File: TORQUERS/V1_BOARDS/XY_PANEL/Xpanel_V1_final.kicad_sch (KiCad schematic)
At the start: 68 parts, among them J2 F3311A7H121014E200, Q1 BSS138, Q10 BSS138, Q11 BSS138, Q13 BSS138, Q14 BSS138, Q2 BSS138, Q4 BSS138, Q5 BSS138, U1 DRV8830DGQ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

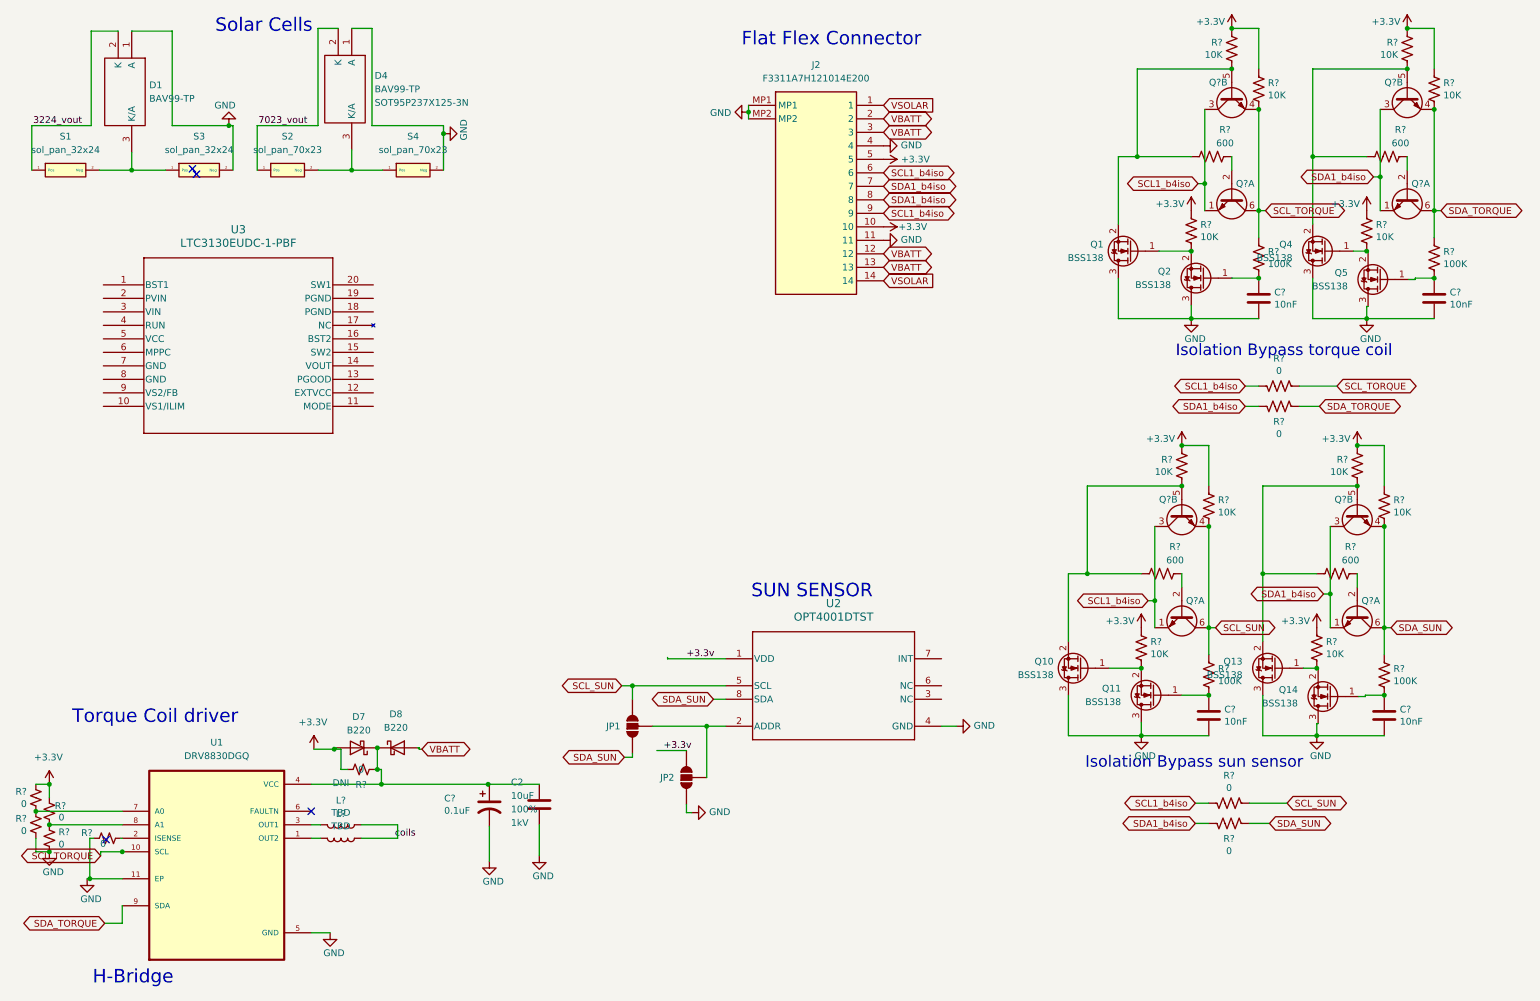
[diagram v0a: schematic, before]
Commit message: Made changes to LTC ; remaining switches for H bridge and  LTC3130 for 70mm panel
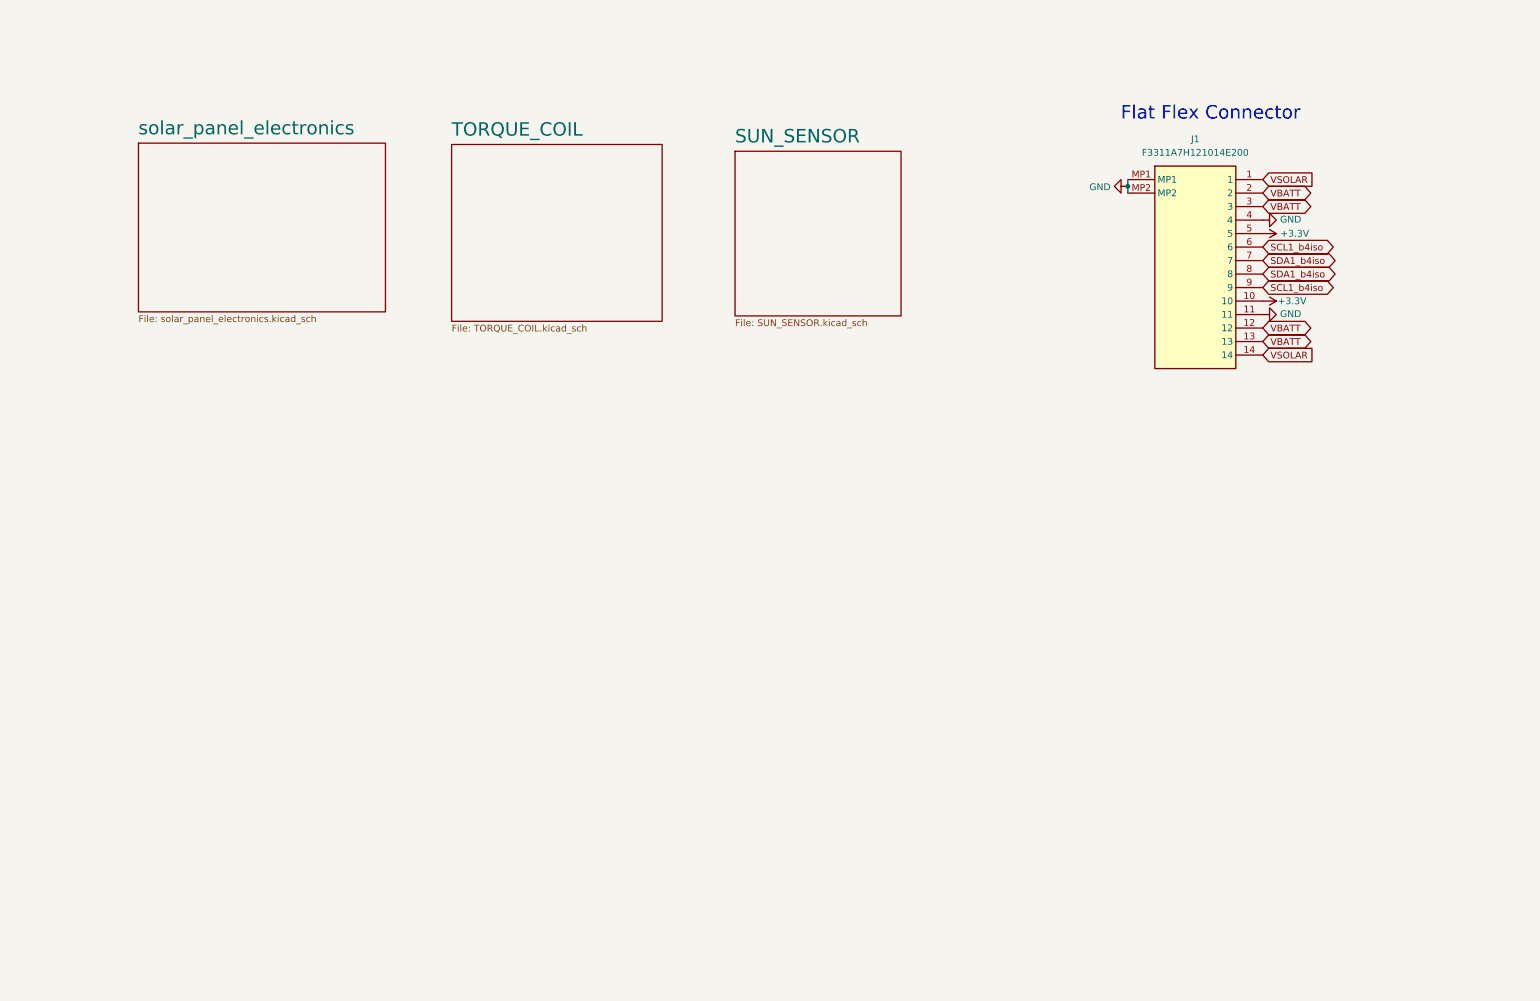
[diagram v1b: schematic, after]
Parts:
- removed C2: 10uF, Capacitor_SMD:C_0805_2012Metric, symbol SparkFun-Capacitor:C_Polarized
- removed C? (x4): 10nF, Capacitor_SMD:C_0603_1608Metric, symbol Device:C
- removed C?: 0.1uF, Capacitor_SMD:C_0402_1005Metric, symbol Device:C
- removed D1, D4: BAV99-TP, SOT95P237X125-3N, symbol AA_AUTO_LOADER:BAV99-TP
- removed D7, D8: B220, Diode_SMD:D_SMB, symbol Diode:B220
- removed J2: F3311A7H121014E200, F3311A7H121014E200, symbol F3311A7H121008E200:F3311A7H121014E200
- removed JP1, JP2: ~, SparkFun-Jumper:SMT-JUMPER_3_NO_NO-SILK, symbol SparkFun-Jumper:SolderJumper_3_Open_No_Silk
- removed L? (x2): TBD, Inductor_SMD:L_0603_1608Metric, symbol Device:L
- removed Q1, Q10, Q11, Q13, Q14, Q2, Q4, Q5: BSS138, Package_TO_SOT_SMD:SOT-23, symbol Transistor_FET:BSS138
- removed Q? (x8): MBT2222ADW1T1, Package_TO_SOT_SMD:SOT-363_SC-70-6, symbol Transistor_BJT:MBT2222ADW1T1
- removed R? (x5): 0, Resistor_SMD:R_0402_1005Metric, symbol Device:R_Small_US
- removed R? (x4): 600, Resistor_SMD:R_0603_1608Metric, symbol Device:R_US
- removed R? (x8): 10K, Resistor_SMD:R_0603_1608Metric, symbol Device:R_US
- removed R?: 0, Resistor_SMD:R_0603_1608Metric, symbol Device:R_Small_US
- removed R? (x4): 0, Resistor_SMD:R_0603_1608Metric, symbol Device:R_US
- removed R? (x4): 100K, Resistor_SMD:R_0603_1608Metric, symbol Device:R_US
- removed R? (x4): 10K, Resistor_SMD:R_0402_1005Metric, symbol Device:R_US
- removed S1, S3: sol_pan_32x24, CUSTOM_SOLAR_2432:solar_panel_SM500K12TF_32x24, symbol solar_symbol_lib:sol_pan_32x24
- removed S2, S4: sol_pan_70x23, CUSTOM_SOLAR_7023:sol_pan_SM141K10TFS_70x23, symbol solar_symbol_lib:sol_pan_70x23
- removed U1: DRV8830DGQ, DRV8830DGQ:IC_XTR111AIDGQR, symbol DRV8830DGQ:DRV8830DGQ
- removed U2: OPT4001DTST, DTS0008A-MFG, symbol OPT4001DTST:OPT4001DTST
- removed U3: LTC3130EUDC-1-PBF, UDC_20_ADI, symbol LTC3130:LTC3130EUDC-1-PBF
- added J1: F3311A7H121014E200, F3311A7H121014E200, symbol F3311A7H121008E200:F3311A7H121014E200
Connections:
- net +3.3V: now also J1.10, J1.5
- net GND: now also J1.11, J1.4, J1.MP1, J1.MP2
- net SCL1_b4iso: now also J1.6, J1.9
- net SDA1_b4iso: now also J1.7, J1.8
- net VBATT: now also J1.12, J1.13, J1.2, J1.3
- net VSOLAR: now also J1.1, J1.14
- no-connect marks 4 -> 0
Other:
- added sheet SUN_SENSOR (SUN_SENSOR.kicad_sch)
- added sheet TORQUE_COIL (TORQUE_COIL.kicad_sch)
- added sheet solar_panel_electronics (solar_panel_electronics.kicad_sch)
- note removed: "H-Bridge"
- note removed: "Isolation Bypass sun sensor"
- note removed: "Isolation Bypass torque coil"
- note removed: "SUN SENSOR"
- note removed: "Solar Cells"
- note removed: "Torque Coil driver"

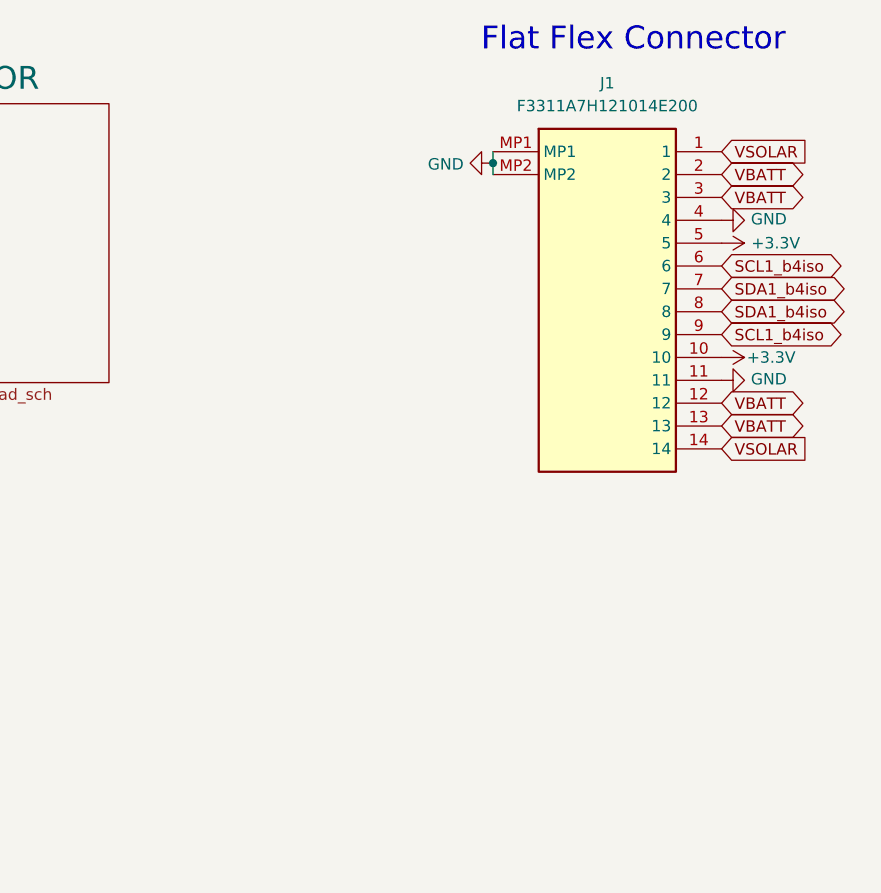
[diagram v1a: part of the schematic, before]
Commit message: completed XY Board
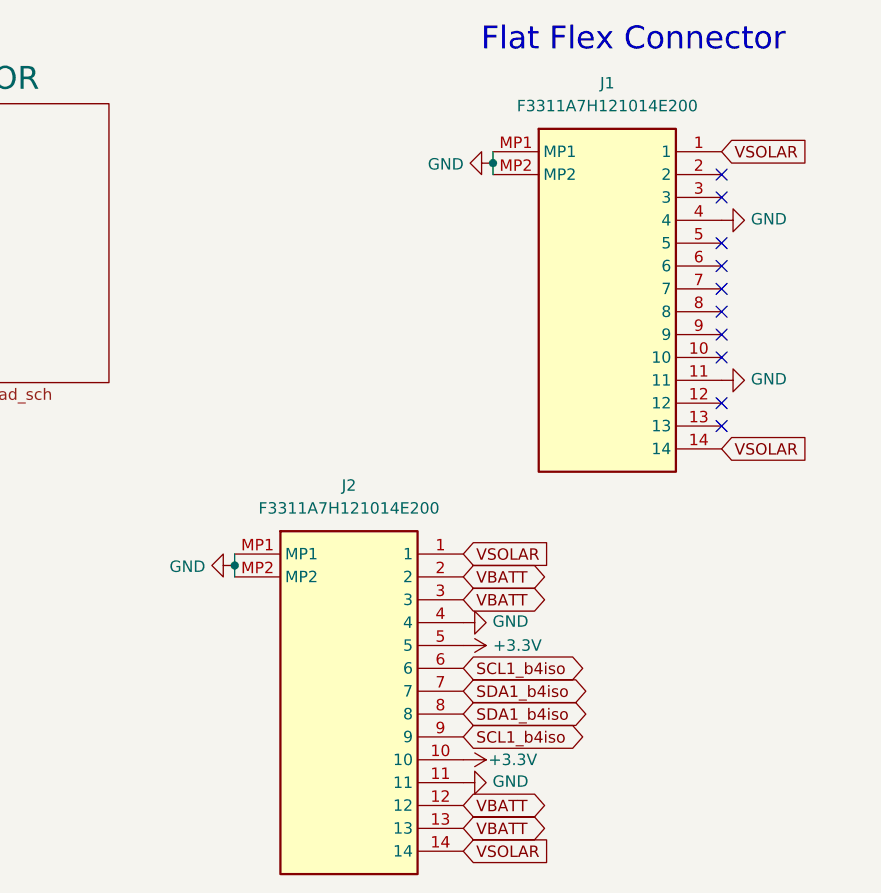
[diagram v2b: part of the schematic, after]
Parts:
- added J2: F3311A7H121014E200, F3311A7H121014E200, symbol F3311A7H121008E200:F3311A7H121014E200
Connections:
- net +3.3V: now also J2.10, J2.5; no longer J1.10, J1.5
- net GND: now also J2.11, J2.4, J2.MP1, J2.MP2
- net SCL1_b4iso: now also J2.6, J2.9; no longer J1.6, J1.9
- net SDA1_b4iso: now also J2.7, J2.8; no longer J1.7, J1.8
- net VBATT: now also J2.12, J2.13, J2.2, J2.3; no longer J1.12, J1.13, J1.2, J1.3
- net VSOLAR: now also J2.1, J2.14
- no-connect marks 0 -> 10
